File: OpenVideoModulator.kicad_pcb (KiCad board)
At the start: 2 copper layers, 32 x 25 mm, 22 parts, among them J1 CONN_6, J2 Conn_Coaxial, P1 OSHW_LOGO, U1 AD724, Y1 4.433619M

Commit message: Almost there...
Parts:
- C6: footprint Capacitor_SMD:C_0805_2012Metric_Pad1.15x1.40mm_HandSolder -> Capacitor_SMD:CP_Elec_6.3x5.8; moved to F.Cu
- C7: footprint Capacitor_SMD:C_0805_2012Metric_Pad1.15x1.40mm_HandSolder -> Capacitor_SMD:C_1206_3216Metric_Pad1.42x1.75mm_HandSolder; moved to F.Cu
- J2: value Conn_Coaxial -> S-Video+Composite_Combo; footprint w_conn_av:rca_yellow -> OpenVideoModulator:AV-MDC-401
- JP1: footprint Jumper:SolderJumper-3_P1.3mm_Open_RoundedPad1.0x1.5mm -> OpenVideoModulator:SolderJumper-3_P1.3mm_Bridged12_RoundedPad1.0x1.5mm
- R4, R5, R6: moved to F.Cu
- Y1: footprint Crystal:Crystal_HC49-U_Vertical -> Crystal:Crystal_HC49-4H_Vertical
- moved R5 19.2 mm to (135.5, 55.8), turned to 180 degrees
- moved C10 19.0 mm to (133.0, 71.6), turned to 90 degrees
- moved P1 13.6 mm to (144.9, 70.9)
- moved J2 12.0 mm to (153.3, 66.5)
- moved R4 11.0 mm to (135.5, 59.1), turned to 180 degrees
- moved C8 10.9 mm to (126.7, 71.6), turned to 90 degrees
- moved C6 10.2 mm to (129.3, 61.5), turned to 270 degrees
- moved JP1 10.0 mm to (121.2, 61.5)
- moved C7 9.45 mm to (124.1, 61.5), turned to 90 degrees
- moved R6 8.85 mm to (135.5, 62.3), turned to 180 degrees
- moved C9 3.94 mm to (120.4, 71.6), turned to 90 degrees
- moved Y1 0.29 mm to (129.4, 52.8)
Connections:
- C5 pad 2: VCC -> VAA
- J1 pad 1: VCC -> VAA
- J2 pad 1: Net-(J2-Pad1) -> GND
- JP1 pad 3: VCC -> VAA
- R4 pad 1: Net-(J2-Pad1) -> Net-(J2-Pad6)
- R5 pad 1: Net-(J3-Pad3) -> Net-(J2-Pad3)
- R6 pad 1: Net-(J3-Pad4) -> Net-(J2-Pad4)
- U1 pad 14: VCC -> VAA
- U1 pad 15: VCC -> VAA
- U1 pad 4: VCC -> VAA
- U1 pad 5: VCC -> VAA
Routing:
- net VCC: track 58.1 -> 0.00 mm
- net VAA: track 3.05 -> 50.8 mm, vias 0 -> 1
- net Net-(J3-Pad3): track 35.8 -> 0.00 mm
- net Net-(C9-Pad2): track 2.90 -> 26.1 mm
- net Net-(C10-Pad1): track 6.66 -> 20.6 mm
- net Net-(C8-Pad2): track 6.68 -> 17.0 mm
- net Net-(C1-Pad1): track 16.0 -> 23.9 mm
- net Net-(C8-Pad1): track 15.2 -> 22.5 mm
- net Net-(J2-Pad4): track 0.00 -> 7.25 mm
- net Net-(J2-Pad3): track 0.00 -> 7.25 mm
- net Net-(J2-Pad6): track 0.00 -> 2.76 mm
- net Net-(C10-Pad2): track 6.04 -> 8.30 mm
- net GND: track 1.75 -> 2.94 mm, vias 5 -> 3
- net Net-(JP1-Pad2): track 13.8 -> 13.1 mm
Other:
- board size 32 x 25 mm -> 38.6 x 24.1 mm
- rule pad_to_mask_clearance: 0.051 -> 0
- rule solder_mask_min_width: 0.25 -> 0.2
- board text added: "Licensed under CERN OHL v.1.2"
- board text added: "V1"

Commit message: Minor fixes
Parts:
- P1: moved to B.Cu
- moved P1 5.42 mm to (140.7, 67.4), turned to 180 degrees
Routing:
- net Net-(C10-Pad1): track 20.6 -> 18.9 mm
- net GND: vias 3 -> 2
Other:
- board text added: "+5V"
- board text added: "B"
- board text added: "G"
- board text added: "GND"
- board text added: "NTSC"
- board text added: "PAL"
- board text added: "R"
- board text added: "SY"
- board text added: "github.com/SukkoPera/ OpenVideoModulator"
- board text removed: "PAL/NTSC"

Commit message: More fixes
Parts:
- moved P1 7.99 mm to (148.1, 70.5)
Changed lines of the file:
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@@
   )
   (module Symbol:OSHW-Logo2_7.3x6mm_Copper (layer B.Cu)
-    (at 140.716 67.437 180)
+    (at 148.082 70.539772 180)
     (descr "Open Source Hardware Symbol")
     (tags "Logo Symbol OSHW")
@@
     (effects (font (size 0.8 0.8) (thickness 0.15)))
   )
-  (gr_text "Licensed under\nCERN OHL v.1.2" (at 144.272 71.882) (layer B.SilkS)
+  (gr_text "Licensed\nunder CERN\nOHL v.1.2" (at 141.097 70.485) (layer B.SilkS)
     (effects (font (size 0.8 0.8) (thickness 0.15)) (justify mirror))
   )

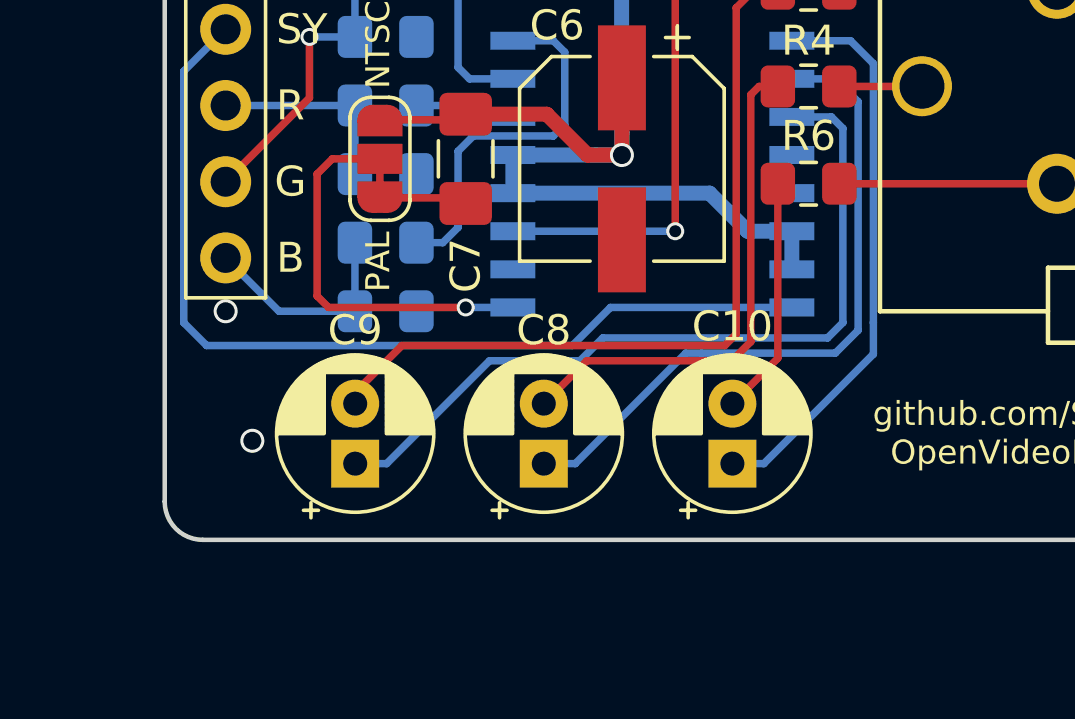
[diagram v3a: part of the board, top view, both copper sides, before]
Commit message: Use 6.3mm electrolytics, as 220uF seem to be more common this size At least >= 16V models, which are recommended
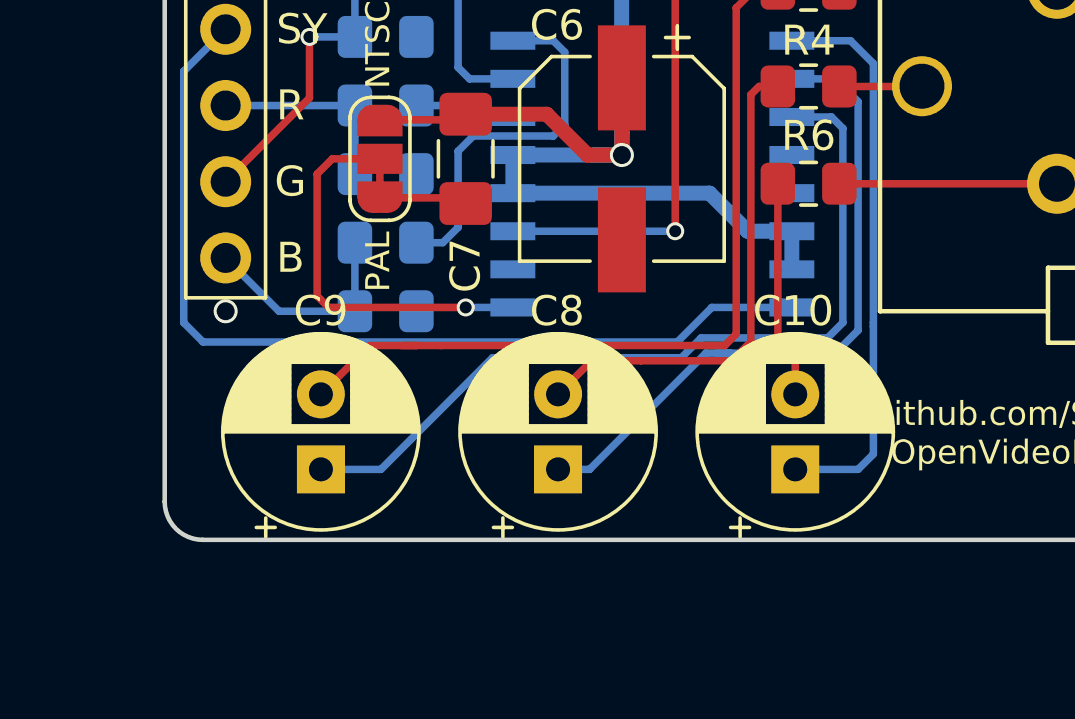
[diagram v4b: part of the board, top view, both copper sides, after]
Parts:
- C10, C8, C9: footprint Capacitor_THT:CP_Radial_D5.0mm_P2.00mm -> Capacitor_THT:CP_Radial_D6.3mm_P2.50mm
- moved C10 2.10 mm to (135.1, 71.8)
- moved C9 1.16 mm to (119.3, 71.8)
- moved C8 0.51 mm to (127.2, 71.8)
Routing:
- net Net-(C9-Pad2): track 26.0 -> 27.7 mm
- net Net-(C9-Pad1): track 26.5 -> 27.8 mm
- net Net-(C10-Pad2): track 8.30 -> 7.26 mm
- net Net-(C8-Pad2): track 17.0 -> 16.4 mm
- net GND: vias 2 -> 1

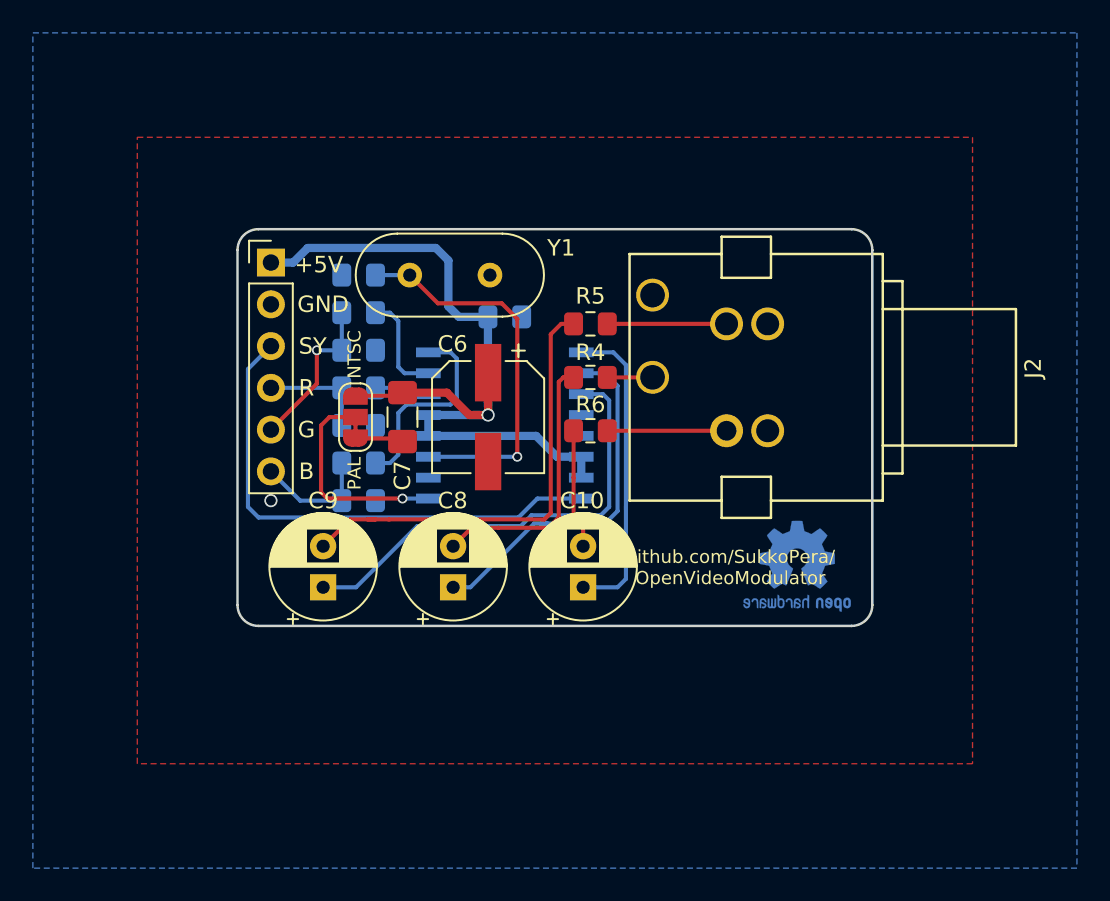
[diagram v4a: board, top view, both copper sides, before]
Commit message: Stitch grounds
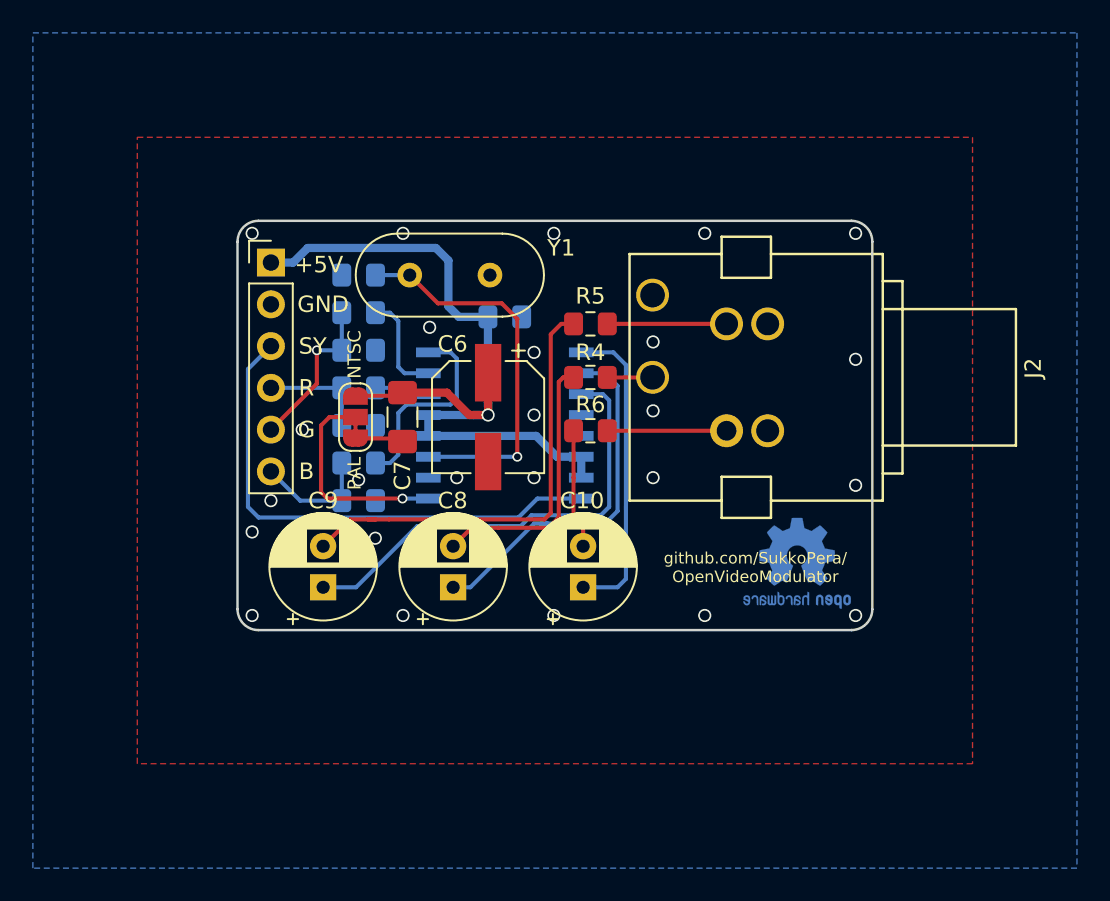
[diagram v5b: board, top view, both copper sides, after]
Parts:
- moved P1 0.18 mm to (148.1, 70.4)
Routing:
- net GND: vias 1 -> 27
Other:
- board size 38.6 x 24.1 mm -> 38.6 x 24.9 mm
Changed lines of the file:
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@@
     (thickness 1.6)
     (drawings 21)
-    (tracks 128)
+    (tracks 154)
     (zones 0)
     (modules 22)
@@
   (title_block
     (title OpenVideoModulator)
-    (date 2019-03-20)
+    (date 2019-03-21)
     (rev 1git)
     (company SukkoPera)
@@
   )
   (module Symbol:OSHW-Logo2_7.3x6mm_Copper (layer B.Cu)
-    (at 148.082 70.539772 180)
+    (at 148.082 70.358 180)
     (descr "Open Source Hardware Symbol")
     (tags "Logo Symbol OSHW")
@@
     (effects (font (size 0.8 0.8) (thickness 0.15)))
   )
-  (gr_text "github.com/SukkoPera/\nOpenVideoModulator" (at 144.018 70.611387) (layer F.SilkS)
-    (effects (font (size 0.8 0.8) (thickness 0.15)))
-  )
-  (gr_text "Licensed\nunder CERN\nOHL v.1.2" (at 141.097 70.485) (layer B.SilkS)
+  (gr_text "github.com/SukkoPera/\nOpenVideoModulator" (at 145.542 70.612) (layer F.SilkS)
+    (effects (font (size 0.7 0.7) (thickness 0.15)))
+  )
+  (gr_text "Licensed\nunder CERN\nOHL v.1.2" (at 141.097 70.104) (layer B.SilkS)
     (effects (font (size 0.8 0.8) (thickness 0.15)) (justify mirror))
   )
-  (gr_text V1 (at 115.57 72.771) (layer B.SilkS)
+  (gr_text V1 (at 116.078 72.517) (layer B.SilkS)
     (effects (font (size 1 1) (thickness 0.2)) (justify mirror))
   )
@@
     (arrow2b (pts (xy 114.046 78.74) (xy 115.172504 78.153579)))
   )
-  (gr_arc (start 115.316 51.308) (end 115.316 50.038) (angle -90) (layer Edge.Cuts) (width 0.15))
-  (gr_arc (start 115.316 72.898) (end 114.046 72.898) (angle -90) (layer Edge.Cuts) (width 0.15))
-  (gr_arc (start 151.384 72.898) (end 151.384 74.168) (angle -90) (layer Edge.Cuts) (width 0.15))
-  (gr_arc (start 151.384 51.308) (end 152.654 51.308) (angle -90) (layer Edge.Cuts) (width 0.15))
+  (gr_arc (start 115.316 50.8) (end 115.316 49.53) (angle -90) (layer Edge.Cuts) (width 0.15))
+  (gr_arc (start 115.316 73.152) (end 114.046 73.152) (angle -90) (layer Edge.Cuts) (width 0.15))
+  (gr_arc (start 151.384 73.152) (end 151.384 74.422) (angle -90) (layer Edge.Cuts) (width 0.15))
+  (gr_arc (start 151.384 50.8) (end 152.654 50.8) (angle -90) (layer Edge.Cuts) (width 0.15))
   (gr_text PAL (at 121.158 64.897 90) (layer F.SilkS)
     (effects (font (size 0.8 0.8) (thickness 0.15)))
   )
-  (gr_line (start 114.046 72.898) (end 114.046 51.308) (layer Edge.Cuts) (width 0.15))
-  (gr_line (start 151.4 74.168) (end 115.316 74.168) (layer Edge.Cuts) (width 0.15))
-  (gr_line (start 152.654 51.308) (end 152.654 72.898) (layer Edge.Cuts) (width 0.15))
-  (gr_line (start 115.316 50.038) (end 151.4 50.038) (layer Edge.Cuts) (width 0.15))
+  (gr_line (start 114.046 73.152) (end 114.046 50.8) (layer Edge.Cuts) (width 0.15))
+  (gr_line (start 151.4 74.422) (end 115.316 74.422) (layer Edge.Cuts) (width 0.15))
+  (gr_line (start 152.654 50.8) (end 152.654 73.152) (layer Edge.Cuts) (width 0.15))
+  (gr_line (start 115.316 49.53) (end 151.4 49.53) (layer Edge.Cuts) (width 0.15))
   (segment (start 124.406 52.832) (end 124.66 53.086) (width 0.25) (layer B.Cu) (net 1) (status 30))
   (segment (start 122.437 52.832) (end 124.52 52.832) (width 0.25) (layer B.Cu) (net 1) (status 30))
@@
   (segment (start 123.8915 62.768) (end 124.079 62.9555) (width 0.25) (layer F.Cu) (net 2))
   (segment (start 121.2215 62.768) (end 123.8915 62.768) (width 0.25) (layer F.Cu) (net 2))
+  (via (at 114.935 73.533) (size 0.8) (drill 0.6) (layers F.Cu B.Cu) (net 2))
+  (via (at 124.11075 73.533) (size 0.8) (drill 0.6) (layers F.Cu B.Cu) (net 2))
+  (via (at 133.2865 73.533) (size 0.8) (drill 0.6) (layers F.Cu B.Cu) (net 2))
+  (via (at 142.46225 73.533) (size 0.8) (drill 0.6) (layers F.Cu B.Cu) (net 2))
+  (via (at 151.638 73.533) (size 0.8) (drill 0.6) (layers F.Cu B.Cu) (net 2))
+  (via (at 151.638 50.292) (size 0.8) (drill 0.6) (layers F.Cu B.Cu) (net 2))
+  (via (at 114.935 50.292) (size 0.8) (drill 0.6) (layers F.Cu B.Cu) (net 2))
+  (via (at 124.11075 50.292) (size 0.8) (drill 0.6) (layers F.Cu B.Cu) (net 2))
+  (via (at 133.2865 50.292) (size 0.8) (drill 0.6) (layers F.Cu B.Cu) (net 2))
+  (via (at 142.46225 50.292) (size 0.8) (drill 0.6) (layers F.Cu B.Cu) (net 2))
+  (via (at 114.935 68.453) (size 0.8) (drill 0.6) (layers F.Cu B.Cu) (net 2))
+  (via (at 151.638 65.616666) (size 0.8) (drill 0.6) (layers F.Cu B.Cu) (net 2))
+  (via (at 151.638 57.954333) (size 0.8) (drill 0.6) (layers F.Cu B.Cu) (net 2))
+  (via (at 122.428 68.834) (size 0.8) (drill 0.6) (layers F.Cu B.Cu) (net 2))
+  (via (at 129.286 69.215) (size 0.8) (drill 0.6) (layers F.Cu B.Cu) (net 2))
+  (via (at 136.652 69.215) (size 0.8) (drill 0.6) (layers F.Cu B.Cu) (net 2))
+  (via (at 117.983 62.23) (size 0.8) (drill 0.6) (layers F.Cu B.Cu) (net 2))
+  (via (at 121.412 65.278) (size 0.8) (drill 0.6) (layers F.Cu B.Cu) (net 2))
+  (via (at 127.381 65.151) (size 0.8) (drill 0.6) (layers F.Cu B.Cu) (net 2))
+  (via (at 132.08 65.151) (size 0.8) (drill 0.6) (layers F.Cu B.Cu) (net 2))
+  (via (at 139.319 65.151) (size 0.8) (drill 0.6) (layers F.Cu B.Cu) (net 2))
+  (via (at 132.08 61.341) (size 0.8) (drill 0.6) (layers F.Cu B.Cu) (net 2))
+  (via (at 125.73 56.007) (size 0.8) (drill 0.6) (layers F.Cu B.Cu) (net 2))
+  (via (at 132.08 57.531) (size 0.8) (drill 0.6) (layers F.Cu B.Cu) (net 2))
+  (via (at 139.319 61.087) (size 0.8) (drill 0.6) (layers F.Cu B.Cu) (net 2))
+  (via (at 139.319 56.896) (size 0.8) (drill 0.6) (layers F.Cu B.Cu) (net 2))
   (segment (start 125.652 60.071) (end 124.206 60.071) (width 0.25) (layer B.Cu) (net 3) (status 10))
   (segment (start 123.825 59.69) (end 122.437 59.69) (width 0.25) (layer B.Cu) (net 3) (status 20))
